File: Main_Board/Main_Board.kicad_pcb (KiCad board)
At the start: 4 copper layers, 45 x 38.4 mm, 128 parts, among them IC1 TPS25200DRVR, J1 RESET, J2 MAIN_UART, J3 Baterry input, J4 External bords interfaces, J7 Terminal, J8 Terminal, Q1 2N7002, Q10 FDN339AN, Q7 MMBT3904LT1G, Q8 FDN339AN, Q9 MMBT3904LT1G, U1 W25Q128JVS, U2 ESP32-S3-MINI-1U, U3 TPS63031DSK, U4 TPS63031DSK, U5 TLV61070ADBV, U6 SS351AT, U7 THVD1450DR

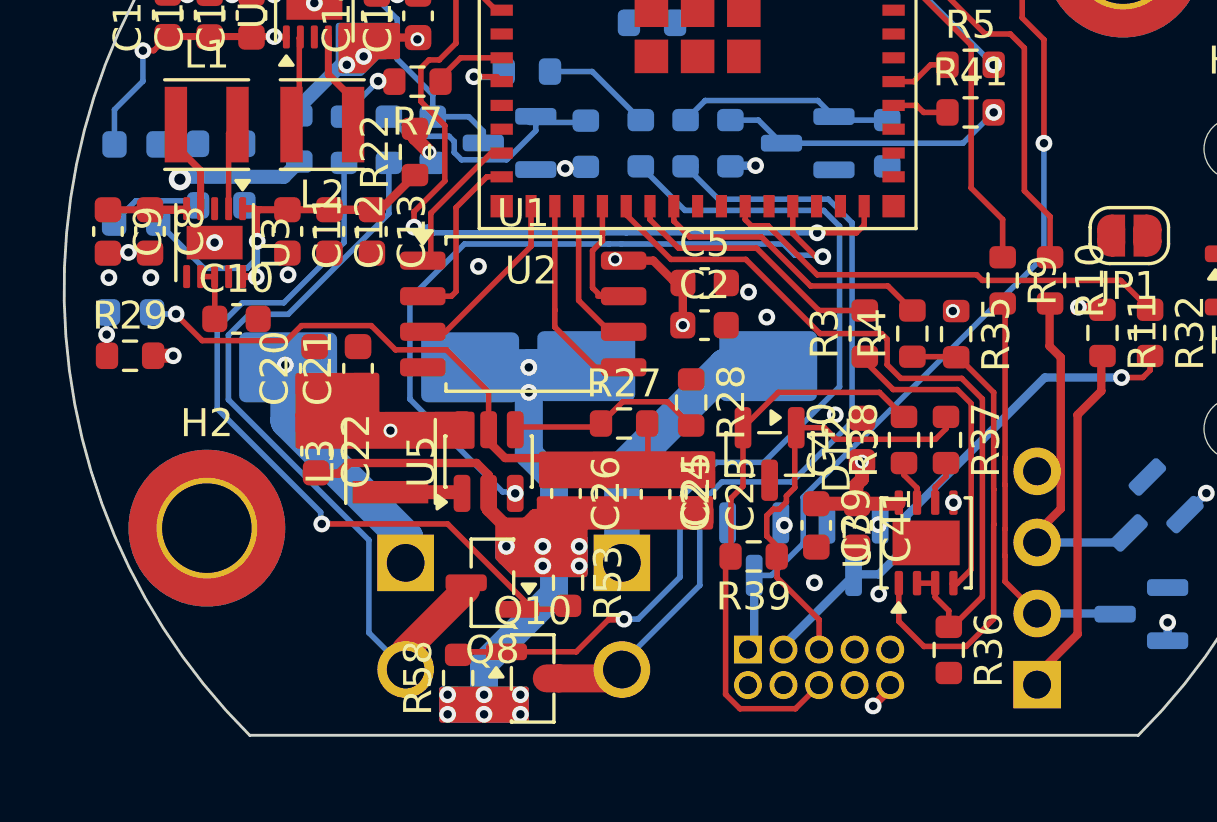
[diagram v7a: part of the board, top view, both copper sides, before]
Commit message: ModuleBus TVS clearance
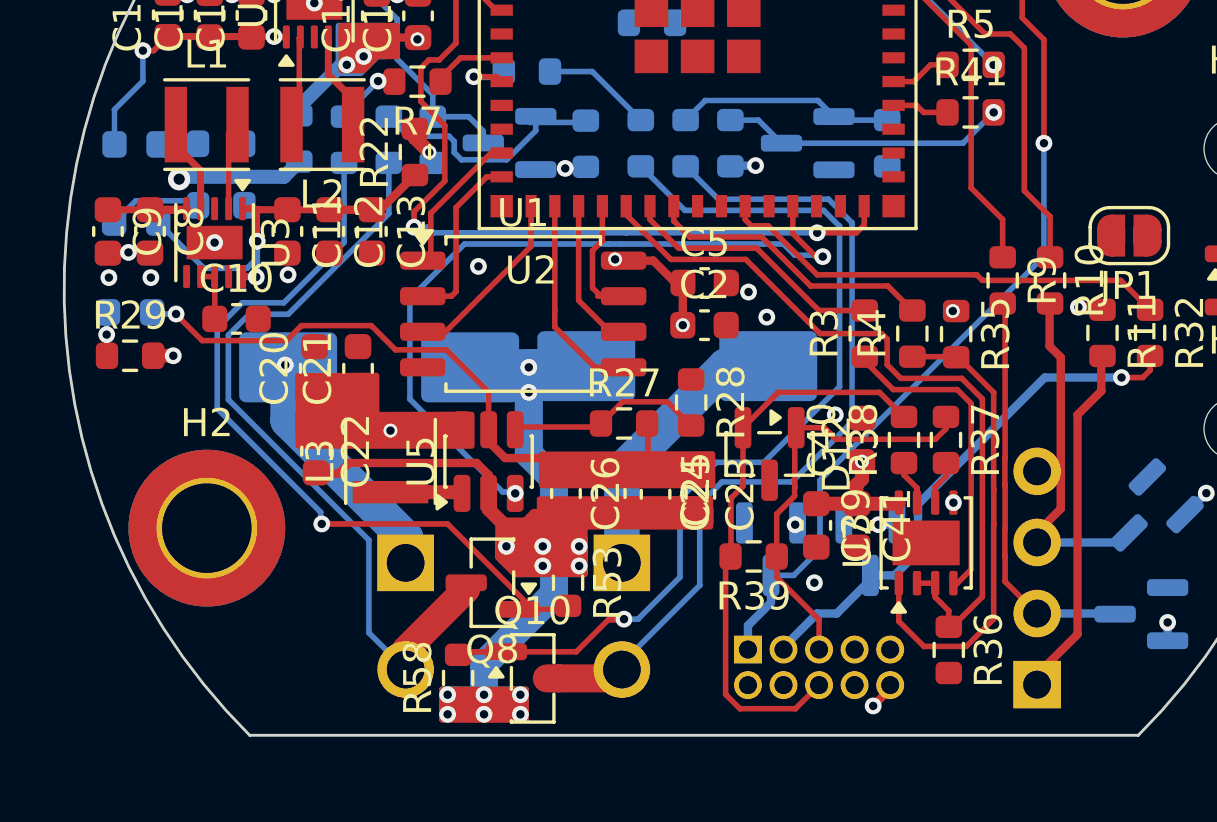
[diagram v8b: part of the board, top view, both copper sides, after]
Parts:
- moved D7 0.60 mm to (102.8, 109.3)
- moved D8 0.60 mm to (106.3, 109.3)
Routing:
- net GND: vias 37 -> 36
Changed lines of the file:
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@@
 	(footprint "Package_TO_SOT_SMD:SOT-23"
 		(layer "B.Cu")
-		(at 105.7 109.3 -90)
+		(at 106.3 109.3 -90)
 		(descr "SOT, 3 Pin (JEDEC TO-236 Var AB https://www.jedec.org/document_search?search_api_views_fulltext=TO-236)")
 		(tags "SOT TO_SOT_SMD")
@@
 	(footprint "Package_TO_SOT_SMD:SOT-23"
 		(layer "B.Cu")
-		(at 102.15 109.3 -90)
+		(at 102.75 109.3 -90)
 		(descr "SOT, 3 Pin (JEDEC TO-236 Var AB https://www.jedec.org/document_search?search_api_views_fulltext=TO-236)")
 		(tags "SOT TO_SOT_SMD")
@@
 	)
 	(via
-		(at 106.6 110.9)
-		(size 0.6)
-		(drill 0.3)
-		(layers "F.Cu" "B.Cu")
-		(free yes)
-		(net "GND")
-	)
-	(via
 		(at 91.2 115.2)
 		(size 0.6)
@@
 	)
 	(segment
-		(start 103.040552 107.875001)
-		(end 102.824999 107.875001)
-		(width 0.2)
-		(layer "F.Cu")
-		(net "/Interfaces/A_RS485")
-	)
-	(segment
 		(start 109 104.575)
 		(end 109 105)
@@
 	)
 	(segment
-		(start 103.3 107.615553)
-		(end 103.040552 107.875001)
+		(start 103.593967 107.406033)
+		(end 103.593967 107.106033)
 		(width 0.2)
 		(layer "F.Cu")
@@
 	)
 	(segment
-		(start 103.3 107.4)
-		(end 103.3 107.615553)
+		(start 102.954798 109.561592)
+		(end 102.954798 108.045202)
 		(width 0.2)
 		(layer "F.Cu")
@@
 	)
 	(segment
-		(start 103.6 105.0125)
-		(end 103.6 107.1)
-		(width 0.2)
-		(layer "F.Cu")
-		(net "/Interfaces/A_RS485")
-	)
-	(segment
 		(start 105.075 105.375)
 		(end 104.6625 104.9625)
@@
 	)
 	(segment
-		(start 103.65 104.9625)
-		(end 103.6 105.0125)
+		(start 102.970629 109.200997)
+		(end 102.970629 109.545761)
 		(width 0.2)
 		(layer "F.Cu")
@@
 	)
 	(segment
-		(start 104.6625 104.9625)
-		(end 103.65 104.9625)
+		(start 102.970629 109.545761)
+		(end 102.954798 109.561592)
 		(width 0.2)
 		(layer "F.Cu")
@@
 	)
 	(segment
-		(start 102.6 108.830368)
-		(end 102.970629 109.200997)
+		(start 103.6 107.1)
+		(end 103.6 105.0125)
 		(width 0.2)
 		(layer "F.Cu")
@@
 	)
 	(segment
-		(start 102.6 108.1)
-		(end 102.6 108.830368)
+		(start 104.6625 104.9625)
+		(end 103.65 104.9625)
 		(width 0.2)
 		(layer "F.Cu")
@@
 	)
 	(segment
-		(start 103.6 107.1)
-		(end 103.3 107.4)
+		(start 103.593967 107.106033)
+		(end 103.6 107.1)
 		(width 0.2)
 		(layer "F.Cu")
@@
 	)
 	(segment
-		(start 102.824999 107.875001)
-		(end 102.6 108.1)
+		(start 103.6 105.0125)
+		(end 103.65 104.9625)
+		(width 0.2)
+		(layer "F.Cu")
+		(net "/Interfaces/A_RS485")
+	)
+	(segment
+		(start 102.954798 108.045202)
+		(end 103.593967 107.406033)
 		(width 0.2)
 		(layer "F.Cu")
@@
 	)
 	(via
-		(at 81.63752 96.084554)
+		(at 81.610606 96.084557)
 		(size 0.8)
 		(drill 0.4)
@@
 	)
 	(segment
-		(start 85.501751 102.805567)
-		(end 85.484251 102.805567)
-		(width 1.27)
-		(layer "B.Cu")
-		(net "VBUS")
-	)
-	(segment
-		(start 81.63752 96.084554)
-		(end 81.722074 96)
+		(start 81.722074 96)
+		(end 85.357685 96)
 		(width 0.5)
 		(layer "B.Cu")
@@
 	)
 	(segment
-		(start 81.722074 96)
-		(end 85.357685 96)
-		(width 0.5)
+		(start 85.501751 102.805567)
+		(end 85.484251 102.805567)
+		(width 1.27)
 		(layer "B.Cu")
 		(net "VBUS")
@@
 	)
 	(segment
-		(start 85.357685 96)
-		(end 85.901907 95.455778)
+		(start 81.610606 96.084557)
+		(end 81.637517 96.084557)
 		(width 0.5)
 		(layer "B.Cu")
@@
 	)
 	(segment
+		(start 85.357685 96)
+		(end 85.901907 95.455778)
+		(width 0.5)
+		(layer "B.Cu")
+		(net "VBUS")
+	)
+	(segment
+		(start 81.637517 96.084557)
+		(end 81.722074 96)
+		(width 0.5)
+		(layer "B.Cu")
+		(net "VBUS")
+	)
+	(segment
 		(start 87.574188 86.696231)
 		(end 90.174698 84.095721)
@@
 	)
 	(via
-		(at 103.227073 108.445273)
+		(at 103.613496 108.426774)
 		(size 0.6)
 		(drill 0.3)
@@
 	)
 	(segment
-		(start 103.227073 108.445273)
+		(start 106.591701 108.425997)
+		(end 106.936503 108.425997)
+		(width 0.3)
+		(layer "B.Cu")
+		(net "+3V3")
+	)
+	(segment
+		(start 106.566702 108.450996)
+		(end 106.550996 108.450996)
+		(width 0.3)
+		(layer "In2.Cu")
+		(net "+3V3")
+	)
+	(segment
+		(start 106.550996 108.450996)
 		(end 106.545273 108.445273)
 		(width 0.3)
@@
 	)
 	(segment
-		(start 106.591701 108.491701)
-		(end 107.507325 109.407325)
+		(start 103.145273 108.445273)
+		(end 103.1 108.4)
 		(width 0.3)
 		(layer "In2.Cu")
@@
 	)
 	(segment
-		(start 106.566702 108.450996)
-		(end 106.591701 108.425997)
+		(start 103.54027 108.5)
+		(end 103.421954 108.5)
 		(width 0.3)
 		(layer "In2.Cu")
@@
 	)
 	(segment
-		(start 106.550996 108.450996)
-		(end 106.566702 108.450996)
+		(start 103.367227 108.445273)
+		(end 103.145273 108.445273)
 		(width 0.3)
 		(layer "In2.Cu")
@@
 	)
 	(segment
-		(start 103.145273 108.445273)
-		(end 103.1 108.4)
+		(start 103.631995 108.445273)
+		(end 103.613496 108.426774)
 		(width 0.3)
 		(layer "In2.Cu")
@@
 	)
 	(segment
-		(start 103.227073 108.445273)
-		(end 103.145273 108.445273)
+		(start 103.421954 108.5)
+		(end 103.367227 108.445273)
 		(width 0.3)
 		(layer "In2.Cu")
@@
 	)
 	(segment
-		(start 106.545273 108.445273)
-		(end 106.550996 108.450996)
+		(start 106.591701 108.491701)
+		(end 107.507325 109.407325)
 		(width 0.3)
 		(layer "In2.Cu")
@@
 	)
 	(segment
-		(start 106.591701 108.425997)
-		(end 106.591701 108.491701)
+		(start 103.613496 108.426774)
+		(end 103.54027 108.5)
 		(width 0.3)
 		(layer "In2.Cu")
@@
 	)
 	(segment
+		(start 106.591701 108.425997)
+		(end 106.566702 108.450996)
+		(width 0.3)
+		(layer "In2.Cu")
+		(net "+3V3")
+	)
+	(segment
+		(start 106.591701 108.425997)
+		(end 106.591701 108.491701)
+		(width 0.3)
+		(layer "In2.Cu")
+		(net "+3V3")
+	)
+	(segment
+		(start 106.545273 108.445273)
+		(end 103.631995 108.445273)
+		(width 0.3)
+		(layer "In2.Cu")
+		(net "+3V3")
+	)
+	(segment
 		(start 109.15 83.4375)
 		(end 109.15 85.325)
@@
 	)
 	(segment
-		(start 107.6 109.2)
-		(end 107.6 108.1)
-		(width 0.3)
+		(start 115.272093 103.170527)
+		(end 115.24262 103.2)
+		(width 0.2)
 		(layer "B.Cu")
 		(net "Net-(J4-Pin_3)")
 	)
 	(segment
-		(start 115.272093 103.170527)
-		(end 115.24262 103.2)
-		(width 0.2)
+		(start 105.1 111.6)
+		(end 106.462499 110.237501)
+		(width 0.3)
 		(layer "B.Cu")
 		(net "Net-(J4-Pin_3)")
 	)
 	(segment
-		(start 106.6 110.2)
-		(end 107.6 109.2)
+		(start 112.529473 103.170527)
+		(end 115.272093 103.170527)
 		(width 0.3)
 		(layer "B.Cu")
@@
 	)
 	(segment
-		(start 103.197328 112.740173)
-		(end 103.197328 112.886052)
+		(start 108 109.4)
+		(end 108 107.7)
 		(width 0.3)
 		(layer "B.Cu")
@@
 	)
 	(segment
-		(start 107.6 108.1)
-		(end 112.529473 103.170527)
+		(start 103.197328 112.802672)
+		(end 104.4 111.6)
 		(width 0.3)
 		(layer "B.Cu")
@@
 	)
 	(segment
-		(start 105.7 110.1)
-		(end 105.8 110.2)
+		(start 108 107.7)
+		(end 112.529473 103.170527)
 		(width 0.3)
 		(layer "B.Cu")
@@
 	)
 	(segment
-		(start 105.7 110.237501)
-		(end 103.197328 112.740173)
+		(start 107.162499 110.237501)
+		(end 108 109.4)
 		(width 0.3)
 		(layer "B.Cu")
@@
 	)
 	(segment
-		(start 105.8 110.2)
-		(end 106.6 110.2)
+		(start 103.197328 112.886052)
+		(end 103.197328 112.802672)
 		(width 0.3)
 		(layer "B.Cu")
@@
 	)
 	(segment
-		(start 112.529473 103.170527)
-		(end 115.272093 103.170527)
+		(start 104.4 111.6)
+		(end 105.1 111.6)
 		(width 0.3)
 		(layer "B.Cu")
@@
 	)
 	(segment
-		(start 105.7 110.237501)
-		(end 105.7 110.1)
+		(start 106.462499 110.237501)
+		(end 107.162499 110.237501)
 		(width 0.3)
 		(layer "B.Cu")
@@
 	)
 	(segment
-		(start 103.9 109.1)
+		(start 103.562499 110.237501)
 		(end 102.762499 110.237501)
 		(width 0.2)
@@
 	)
 	(segment
-		(start 102.15 110.237501)
-		(end 102.15 112.663379)
-		(width 0.3)
+		(start 104.5 109.3)
+		(end 103.562499 110.237501)
+		(width 0.2)
 		(layer "B.Cu")
 		(net "Net-(J4-Pin_1)")
 	)
 	(segment
-		(start 102.15 112.663379)
-		(end 101.927327 112.886052)
+		(start 112.5 98.842224)
+		(end 104.5 106.842224)
+		(width 0.2)
+		(layer "B.Cu")
+		(net "Net-(J4-Pin_1)")
+	)
+	(segment
+		(start 102.75 110.237501)
+		(end 102.75 111.20669)
 		(width 0.3)
 		(layer "B.Cu")
@@
 	)
 	(segment
-		(start 112.5 98.842224)
-		(end 103.9 107.442224)
+		(start 104.5 106.842224)
+		(end 104.5 109.3)
 		(width 0.2)
 		(layer "B.Cu")
@@
 	)
 	(segment
-		(start 112.5 94.8)
-		(end 112.5 98.842224)
-		(width 0.2)
+		(start 102.75 111.20669)
+		(end 101.927327 112.029363)
+		(width 0.3)
 		(layer "B.Cu")
 		(net "Net-(J4-Pin_1)")
 	)
 	(segment
-		(start 103.9 107.442224)
-		(end 103.9 109.1)
+		(start 112.5 94.8)
+		(end 112.5 98.842224)
 		(width 0.2)
 		(layer "B.Cu")
@@
 	)
 	(segment
-		(start 102.762499 110.237501)
-		(end 102.15 110.237501)
-		(width 0.2)
+		(start 101.927327 112.029363)
+		(end 101.927327 112.886052)
+		(width 0.3)
 		(layer "B.Cu")
 		(net "Net-(J4-Pin_1)")
